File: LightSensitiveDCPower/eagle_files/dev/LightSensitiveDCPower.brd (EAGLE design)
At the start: 12 x 17.5 mm, 5 parts, among them SW1 PCM12SMTR

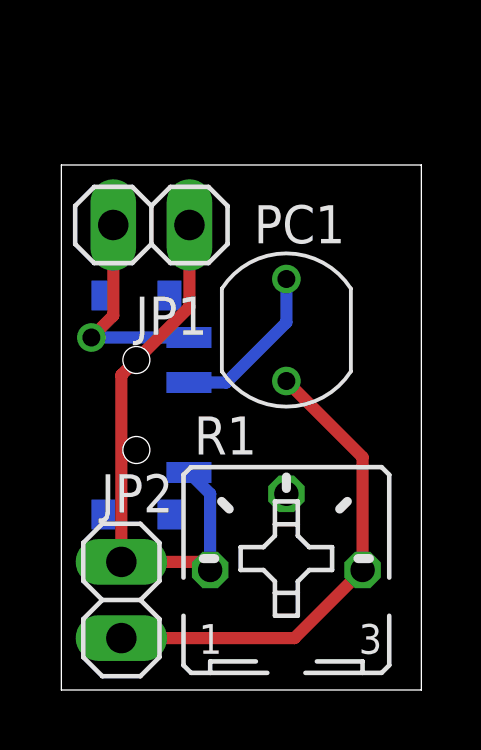
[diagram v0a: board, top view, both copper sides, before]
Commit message: Re-place parts with readjusted text and new labels
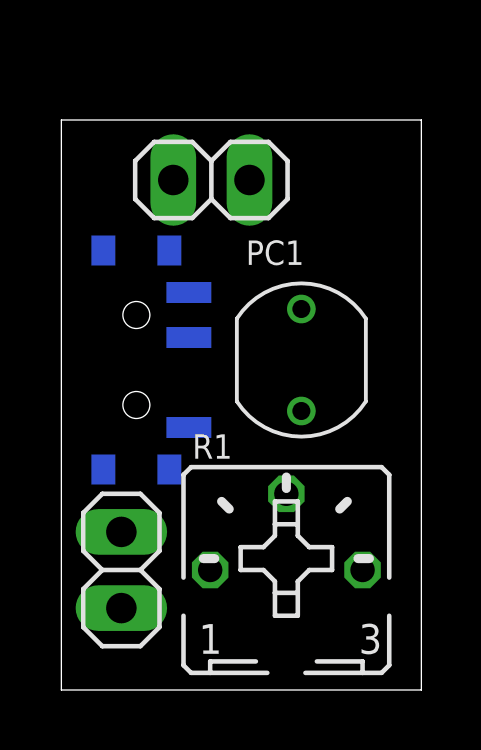
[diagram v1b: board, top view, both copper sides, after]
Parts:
- removed JP1, JP2: (no value), pinhead:1X02
- added IN, OUT: (no value), pinhead:1X02
- moved SW1 1.50 mm to (2.50, 11.0)
- moved PC1 1.12 mm to (8.00, 11.0)
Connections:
- net N$1: now also IN.1, OUT.1; no longer JP1.1, JP2.1
- net N$2: now also IN.2; no longer JP1.2
- net N$5: now also OUT.2; no longer JP2.2
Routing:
- net N$1: track 18.8 -> 0.00 mm
- net N$5: track 16.3 -> 0.00 mm
- net N$2: track 7.30 -> 0.00 mm, vias 1 -> 0
- net N$3: track 5.53 -> 0.00 mm
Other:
- board size 12 x 17.5 mm -> 12 x 19 mm
- board text added: "GND"
- board text added: "VIN"
- board text added: "VOUT"
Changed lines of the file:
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@@
 <layer number="37" name="tTest" color="7" fill="1" visible="no" active="yes"/>
 <layer number="38" name="bTest" color="7" fill="1" visible="no" active="yes"/>
-<layer number="39" name="tKeepout" color="4" fill="11" visible="yes" active="yes"/>
+<layer number="39" name="tKeepout" color="4" fill="11" visible="no" active="yes"/>
 <layer number="40" name="bKeepout" color="1" fill="11" visible="yes" active="yes"/>
 <layer number="41" name="tRestrict" color="4" fill="10" visible="yes" active="yes"/>
@@
 <plain>
 <wire x1="0" y1="0" x2="12" y2="0" width="0" layer="20"/>
-<wire x1="12" y1="0" x2="12" y2="17.5" width="0" layer="20"/>
-<wire x1="12" y1="17.5" x2="0" y2="17.5" width="0" layer="20"/>
-<wire x1="0" y1="17.5" x2="0" y2="0" width="0" layer="20"/>
+<wire x1="12" y1="0" x2="12" y2="19" width="0" layer="20"/>
+<wire x1="12" y1="19" x2="0" y2="19" width="0" layer="20"/>
+<wire x1="0" y1="19" x2="0" y2="0" width="0" layer="20"/>
+<text x="0.7" y="17.69" size="0.6096" layer="51">VIN</text>
+<text x="1.11" y="6.92" size="0.6096" layer="51">VOUT</text>
+<text x="1.13" y="0.5" size="0.6096" layer="51">GND</text>
+<text x="8.07" y="17.65" size="0.6096" layer="51">GND</text>
 </plain>
 <attributes>
@@
 </autorouter>
 <elements>
-<element name="JP1" library="pinhead" package="1X02" value="" x="3" y="15.5" smashed="yes" rot="R180">
-<attribute name="NAME" x="4.8662" y="13.1112" size="1.27" layer="25" ratio="10" rot="R180"/>
-<attribute name="VALUE" x="5.54" y="18.675" size="1.27" layer="27" rot="R180"/>
-</element>
-<element name="JP2" library="pinhead" package="1X02" value="" x="2" y="3" smashed="yes" rot="R270">
-<attribute name="NAME" x="3.7262" y="7.1912" size="1.27" layer="25" ratio="10" rot="R180"/>
-<attribute name="VALUE" x="-1.175" y="5.54" size="1.27" layer="27" rot="R270"/>
-</element>
-<element name="PC1" library="freddyLibr" package="PHOTOCELL_CERAMIC" value="" x="7.5" y="12" smashed="yes">
-<attribute name="NAME" x="6.42" y="14.89" size="1.27" layer="25"/>
+<element name="IN" library="pinhead" package="1X02" value="" x="5" y="17" smashed="yes" rot="R180">
+<attribute name="VALUE" x="7.54" y="20.175" size="1.27" layer="27" rot="R180"/>
+</element>
+<element name="OUT" library="pinhead" package="1X02" value="" x="2" y="4" smashed="yes" rot="R270">
+<attribute name="VALUE" x="-1.175" y="6.54" size="1.27" layer="27" rot="R270"/>
+</element>
+<element name="PC1" library="freddyLibr" package="PHOTOCELL_CERAMIC" value="" x="8" y="11" smashed="yes">
+<attribute name="NAME" x="6.15" y="14.17" size="0.8128" layer="25"/>
 </element>
 <element name="R1" library="pot" package="B25P" value="" x="7.5" y="4" smashed="yes">
-<attribute name="NAME" x="4.425" y="7.85" size="1.27" layer="25" ratio="10"/>
+<attribute name="NAME" x="4.365" y="7.71" size="0.8128" layer="25" ratio="10"/>
 <attribute name="VALUE" x="4.3504" y="-1.08" size="1.27" layer="27" ratio="10"/>
 </element>
-<element name="SW1" library="freddyLibr" package="PCM12SMTR" value="PCM12SMTR" x="2.5" y="9.5" smashed="yes" rot="MR90">
-<attribute name="NAME" x="4.09" y="14.38" size="1.27" layer="26" rot="MR0"/>
+<element name="SW1" library="freddyLibr" package="PCM12SMTR" value="PCM12SMTR" x="2.5" y="11" smashed="yes" rot="MR90">
+<attribute name="NAME" x="7.48" y="9.6" size="0.8128" layer="26" rot="MR0"/>
 </element>
 </elements>
 <signals>
 <signal name="N$1">
-<contactref element="JP1" pad="1"/>
+<contactref element="IN" pad="1"/>
 <contactref element="SW1" pad="1"/>
 <contactref element="R1" pad="A"/>
-<contactref element="JP2" pad="1"/>
-<wire x1="4.27" y1="15.5" x2="4.27" y2="12.77" width="0.4064" layer="1"/>
-<wire x1="4.27" y1="12.77" x2="2" y2="10.5" width="0.4064" layer="1"/>
-<wire x1="2" y1="10.5" x2="2" y2="4.27" width="0.4064" layer="1"/>
-<wire x1="2" y1="4.27" x2="4.69" y2="4.27" width="0.4064" layer="1"/>
-<wire x1="4.69" y1="4.27" x2="4.96" y2="4" width="0.4064" layer="1"/>
-<wire x1="4.96" y1="4" x2="4.96" y2="6.54" width="0.4064" layer="16"/>
-<wire x1="4.96" y1="6.54" x2="4.25" y2="7.25" width="0.4064" layer="16"/>
+<contactref element="OUT" pad="1"/>
+<wire x1="4.25" y1="8.75" x2="6.27" y2="17" width="0" layer="19" extent="16-16"/>
+<wire x1="4.96" y1="4" x2="4.25" y2="8.75" width="0" layer="19" extent="16-16"/>
+<wire x1="2" y1="5.27" x2="4.96" y2="4" width="0" layer="19" extent="1-1"/>
 </signal>
 <signal name="N$2">
-<contactref element="JP1" pad="2"/>
+<contactref element="IN" pad="2"/>
 <contactref element="SW1" pad="3"/>
-<wire x1="1.73" y1="15.5" x2="1.73" y2="12.48" width="0.4064" layer="1"/>
-<wire x1="1.73" y1="12.48" x2="1" y2="11.75" width="0.4064" layer="1"/>
-<via x="1" y="11.75" extent="1-16" drill="0.6"/>
-<wire x1="1" y1="11.75" x2="4.25" y2="11.75" width="0.4064" layer="16"/>
+<wire x1="4.25" y1="13.25" x2="3.73" y2="17" width="0" layer="19" extent="16-16"/>
 </signal>
 <signal name="N$3">
 <contactref element="SW1" pad="2"/>
 <contactref element="PC1" pad="1"/>
-<wire x1="7.5" y1="13.7" x2="7.5" y2="12.25" width="0.4064" layer="16"/>
-<wire x1="7.5" y1="12.25" x2="5.5" y2="10.25" width="0.4064" layer="16"/>
-<wire x1="5.5" y1="10.25" x2="4.25" y2="10.25" width="0.4064" layer="16"/>
+<wire x1="4.25" y1="11.75" x2="8" y2="12.7" width="0" layer="19" extent="16-16"/>
 </signal>
 <signal name="N$5">
 <contactref element="PC1" pad="2"/>
 <contactref element="R1" pad="E"/>
-<contactref element="JP2" pad="2"/>
-<wire x1="2" y1="1.73" x2="7.77" y2="1.73" width="0.4064" layer="1"/>
-<wire x1="7.77" y1="1.73" x2="10.04" y2="4" width="0.4064" layer="1"/>
-<wire x1="10.04" y1="4" x2="10.04" y2="7.76" width="0.4064" layer="1"/>
-<wire x1="10.04" y1="7.76" x2="7.5" y2="10.3" width="0.4064" layer="1"/>
+<contactref element="OUT" pad="2"/>
+<wire x1="10.04" y1="4" x2="8" y2="9.3" width="0" layer="19" extent="1-1"/>
+<wire x1="2" y1="2.73" x2="10.04" y2="4" width="0" layer="19" extent="1-1"/>
 </signal>
 </signals>

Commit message: Further rearranging and resizing.
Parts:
- moved IN 2.28 mm to (6.67, 15.4)
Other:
- board size 12 x 19 mm -> 12 x 17.5 mm
- board text added: "LiSePow Rev1 09/19/14"
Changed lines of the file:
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@@
 <plain>
 <wire x1="0" y1="0" x2="12" y2="0" width="0" layer="20"/>
-<wire x1="12" y1="0" x2="12" y2="19" width="0" layer="20"/>
-<wire x1="12" y1="19" x2="0" y2="19" width="0" layer="20"/>
-<wire x1="0" y1="19" x2="0" y2="0" width="0" layer="20"/>
-<text x="0.7" y="17.69" size="0.6096" layer="51">VIN</text>
+<wire x1="12" y1="0" x2="12" y2="17.5" width="0" layer="20"/>
+<wire x1="12" y1="17.5" x2="0" y2="17.5" width="0" layer="20"/>
+<wire x1="0" y1="17.5" x2="0" y2="0" width="0" layer="20"/>
+<text x="2.53" y="13.91" size="0.6096" layer="51">VIN</text>
 <text x="1.11" y="6.92" size="0.6096" layer="51">VOUT</text>
 <text x="1.13" y="0.5" size="0.6096" layer="51">GND</text>
-<text x="8.07" y="17.65" size="0.6096" layer="51">GND</text>
+<text x="9.24" y="13.82" size="0.6096" layer="51">GND</text>
+<text x="0.63" y="15.38" size="0.4064" layer="51">LiSePow
+Rev1
+09/19/14</text>
 </plain>
 <attributes>
@@
 </autorouter>
 <elements>
-<element name="IN" library="pinhead" package="1X02" value="" x="5" y="17" smashed="yes" rot="R180">
-<attribute name="VALUE" x="7.54" y="20.175" size="1.27" layer="27" rot="R180"/>
+<element name="IN" library="pinhead" package="1X02" value="" x="6.67" y="15.45" smashed="yes" rot="R180">
+<attribute name="VALUE" x="9.21" y="18.625" size="1.27" layer="27" rot="R180"/>
 </element>
 <element name="OUT" library="pinhead" package="1X02" value="" x="2" y="4" smashed="yes" rot="R270">
@@
 </element>
 <element name="PC1" library="freddyLibr" package="PHOTOCELL_CERAMIC" value="" x="8" y="11" smashed="yes">
-<attribute name="NAME" x="6.15" y="14.17" size="0.8128" layer="25"/>
+<attribute name="NAME" x="3.48" y="12.67" size="0.8128" layer="25"/>
 </element>
 <element name="R1" library="pot" package="B25P" value="" x="7.5" y="4" smashed="yes">
@@
 </element>
 <element name="SW1" library="freddyLibr" package="PCM12SMTR" value="PCM12SMTR" x="2.5" y="11" smashed="yes" rot="MR90">
-<attribute name="NAME" x="7.48" y="9.6" size="0.8128" layer="26" rot="MR0"/>
+<attribute name="NAME" x="6.49" y="9.89" size="0.8128" layer="26" rot="MR0"/>
 </element>
 </elements>
@@
 <contactref element="R1" pad="A"/>
 <contactref element="OUT" pad="1"/>
-<wire x1="4.25" y1="8.75" x2="6.27" y2="17" width="0" layer="19" extent="16-16"/>
+<wire x1="4.25" y1="8.75" x2="7.94" y2="15.45" width="0" layer="19" extent="16-16"/>
 <wire x1="4.96" y1="4" x2="4.25" y2="8.75" width="0" layer="19" extent="16-16"/>
 <wire x1="2" y1="5.27" x2="4.96" y2="4" width="0" layer="19" extent="1-1"/>
@@
 <contactref element="IN" pad="2"/>
 <contactref element="SW1" pad="3"/>
-<wire x1="4.25" y1="13.25" x2="3.73" y2="17" width="0" layer="19" extent="16-16"/>
+<wire x1="4.25" y1="13.25" x2="5.4" y2="15.45" width="0" layer="19" extent="16-16"/>
 </signal>
 <signal name="N$3">
@@
 </board>
 </drawing>
+<compatibility>
+<note version="6.3" minversion="6.2.2" severity="warning">
+Since Version 6.2.2 text objects can contain more than one line,
+which will not be processed correctly with this version.
+</note>
+</compatibility>
 </eagle>

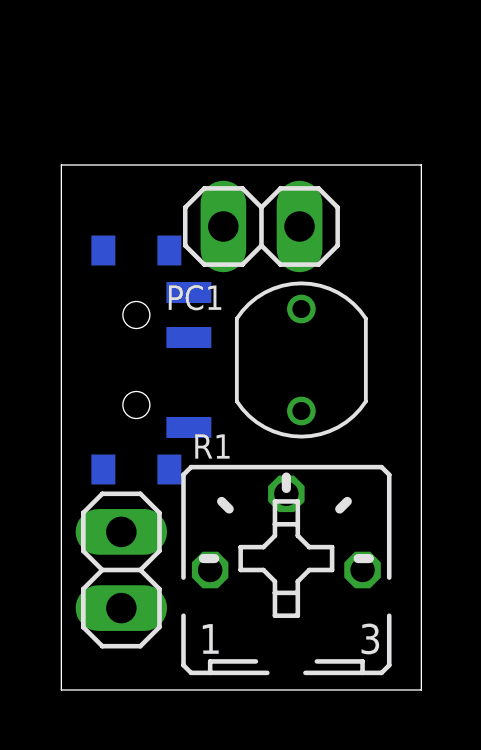
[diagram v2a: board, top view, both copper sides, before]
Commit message: Corrected Pot miswiring. Further rearranging and resizing. I think this is it.
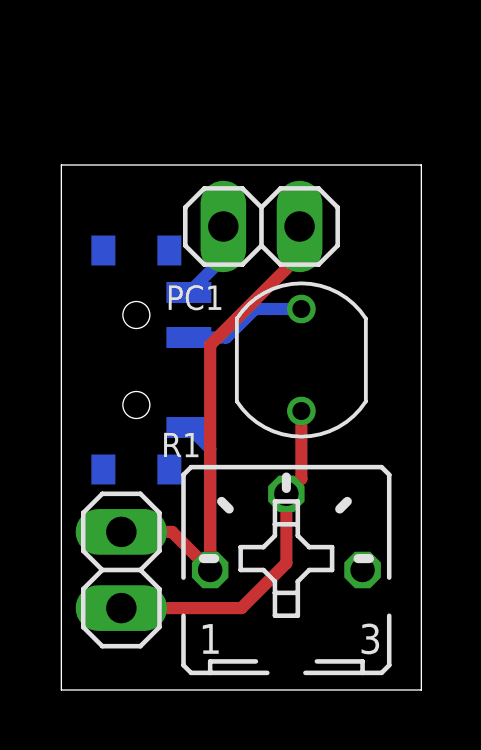
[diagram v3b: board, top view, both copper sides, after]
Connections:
- removed net N$5: OUT.2, PC1.2, R1.E
- new net N$4: OUT.2, PC1.2, R1.S
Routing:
- net N$1: track 0.00 -> 21.2 mm
- net N$4: track 0.00 -> 11.4 mm
- net N$3: track 0.00 -> 4.14 mm
- net N$2: track 0.00 -> 2.68 mm
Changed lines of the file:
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@@
 <wire x1="12" y1="17.5" x2="0" y2="17.5" width="0" layer="20"/>
 <wire x1="0" y1="17.5" x2="0" y2="0" width="0" layer="20"/>
-<text x="2.53" y="13.91" size="0.6096" layer="51">VIN</text>
-<text x="1.11" y="6.92" size="0.6096" layer="51">VOUT</text>
-<text x="1.13" y="0.5" size="0.6096" layer="51">GND</text>
-<text x="9.24" y="13.82" size="0.6096" layer="51">GND</text>
-<text x="0.63" y="15.38" size="0.4064" layer="51">LiSePow
+<text x="2" y="15.25" size="0.6096" layer="51">VIN</text>
+<text x="1.25" y="0.5" size="0.6096" layer="51">VOUT</text>
+<text x="1.25" y="7" size="0.6096" layer="51">GND</text>
+<text x="10" y="15.25" size="0.6096" layer="51">GND</text>
+<text x="1.46" y="10.41" size="0.3048" layer="51">LiSePow
 Rev1
 09/19/14</text>
@@
 </element>
 <element name="R1" library="pot" package="B25P" value="" x="7.5" y="4" smashed="yes">
-<attribute name="NAME" x="4.365" y="7.71" size="0.8128" layer="25" ratio="10"/>
+<attribute name="NAME" x="3.325" y="7.76" size="0.8128" layer="25" ratio="10"/>
 <attribute name="VALUE" x="4.3504" y="-1.08" size="1.27" layer="27" ratio="10"/>
 </element>
 <element name="SW1" library="freddyLibr" package="PCM12SMTR" value="PCM12SMTR" x="2.5" y="11" smashed="yes" rot="MR90">
-<attribute name="NAME" x="6.49" y="9.89" size="0.8128" layer="26" rot="MR0"/>
+<attribute name="NAME" x="3.13" y="15.63" size="0.8128" layer="26" rot="MR0"/>
 </element>
 </elements>
@@
 <contactref element="R1" pad="A"/>
 <contactref element="OUT" pad="1"/>
-<wire x1="4.25" y1="8.75" x2="7.94" y2="15.45" width="0" layer="19" extent="16-16"/>
-<wire x1="4.96" y1="4" x2="4.25" y2="8.75" width="0" layer="19" extent="16-16"/>
-<wire x1="2" y1="5.27" x2="4.96" y2="4" width="0" layer="19" extent="1-1"/>
+<wire x1="2" y1="5.27" x2="3.69" y2="5.27" width="0.4064" layer="1"/>
+<wire x1="3.69" y1="5.27" x2="4.96" y2="4" width="0.4064" layer="1"/>
+<wire x1="4.96" y1="4" x2="4.96" y2="8.04" width="0.4064" layer="16"/>
+<wire x1="4.96" y1="8.04" x2="4.25" y2="8.75" width="0.4064" layer="16"/>
+<wire x1="7.94" y1="15.45" x2="7.94" y2="14.48" width="0.4064" layer="1"/>
+<wire x1="7.94" y1="14.48" x2="4.96" y2="11.5" width="0.4064" layer="1"/>
+<wire x1="4.96" y1="11.5" x2="4.96" y2="4" width="0.4064" layer="1"/>
 </signal>
 <signal name="N$2">
 <contactref element="IN" pad="2"/>
 <contactref element="SW1" pad="3"/>
-<wire x1="4.25" y1="13.25" x2="5.4" y2="15.45" width="0" layer="19" extent="16-16"/>
+<wire x1="5.4" y1="15.45" x2="5.4" y2="14.4" width="0.4064" layer="16"/>
+<wire x1="5.4" y1="14.4" x2="4.25" y2="13.25" width="0.4064" layer="16"/>
 </signal>
 <signal name="N$3">
 <contactref element="SW1" pad="2"/>
 <contactref element="PC1" pad="1"/>
-<wire x1="4.25" y1="11.75" x2="8" y2="12.7" width="0" layer="19" extent="16-16"/>
-</signal>
-<signal name="N$5">
+<wire x1="8" y1="12.7" x2="6.45" y2="12.7" width="0.4064" layer="16"/>
+<wire x1="6.45" y1="12.7" x2="5.5" y2="11.75" width="0.4064" layer="16"/>
+<wire x1="5.5" y1="11.75" x2="4.25" y2="11.75" width="0.4064" layer="16"/>
+</signal>
+<signal name="N$4">
+<contactref element="R1" pad="S"/>
+<contactref element="OUT" pad="2"/>
 <contactref element="PC1" pad="2"/>
-<contactref element="R1" pad="E"/>
-<contactref element="OUT" pad="2"/>
-<wire x1="10.04" y1="4" x2="8" y2="9.3" width="0" layer="19" extent="1-1"/>
-<wire x1="2" y1="2.73" x2="10.04" y2="4" width="0" layer="19" extent="1-1"/>
+<wire x1="8" y1="9.3" x2="8" y2="7.04" width="0.4064" layer="1"/>
+<wire x1="8" y1="7.04" x2="7.5" y2="6.54" width="0.4064" layer="1"/>
+<wire x1="7.5" y1="6.54" x2="7.5" y2="4.23" width="0.4064" layer="1"/>
+<wire x1="7.5" y1="4.23" x2="6" y2="2.73" width="0.4064" layer="1"/>
+<wire x1="6" y1="2.73" x2="2" y2="2.73" width="0.4064" layer="1"/>
 </signal>
 </signals>
